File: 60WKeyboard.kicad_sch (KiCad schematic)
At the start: 59 parts, among them IC2 USBLC6-2SC6, J1 USB4215-03-A_REVA, J2 Conn_02x01_MountingPin, U1 PES12-42S-N0024, U3 nRF52840, Y1 ABM11W-32.0000MHZ-7-D1X-T3, Y2 ECS-.327-7-12-TR

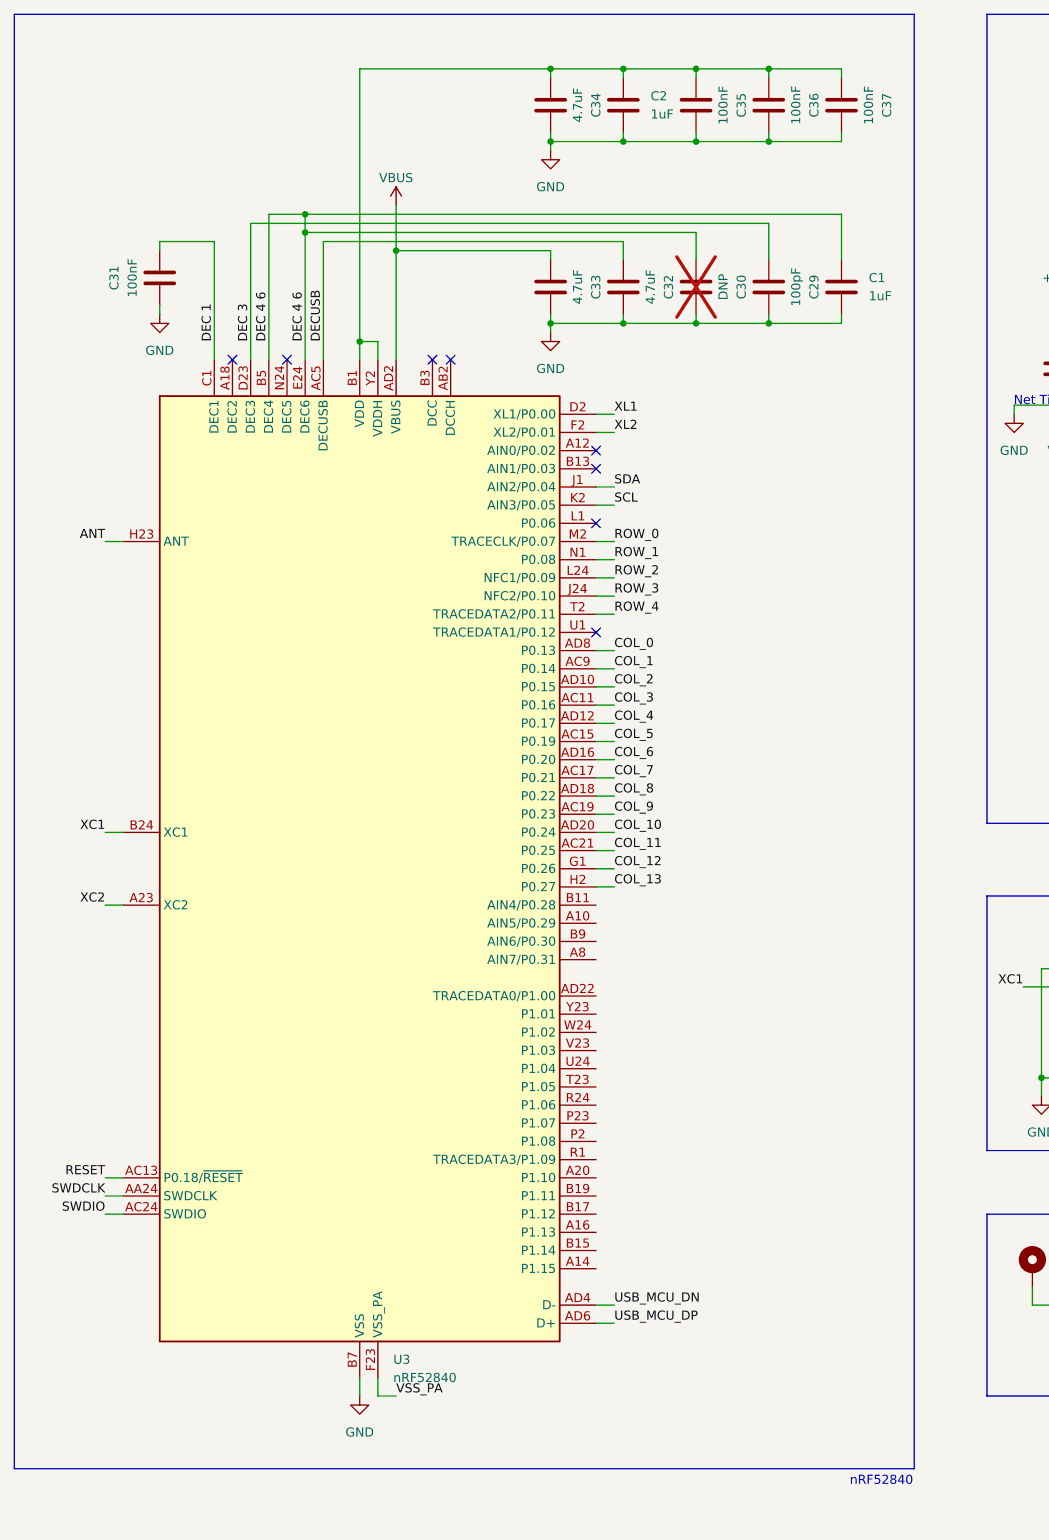
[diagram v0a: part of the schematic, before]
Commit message: v0.3
mcu power traces done
moving onto pmic
then connect key matrix
then done?
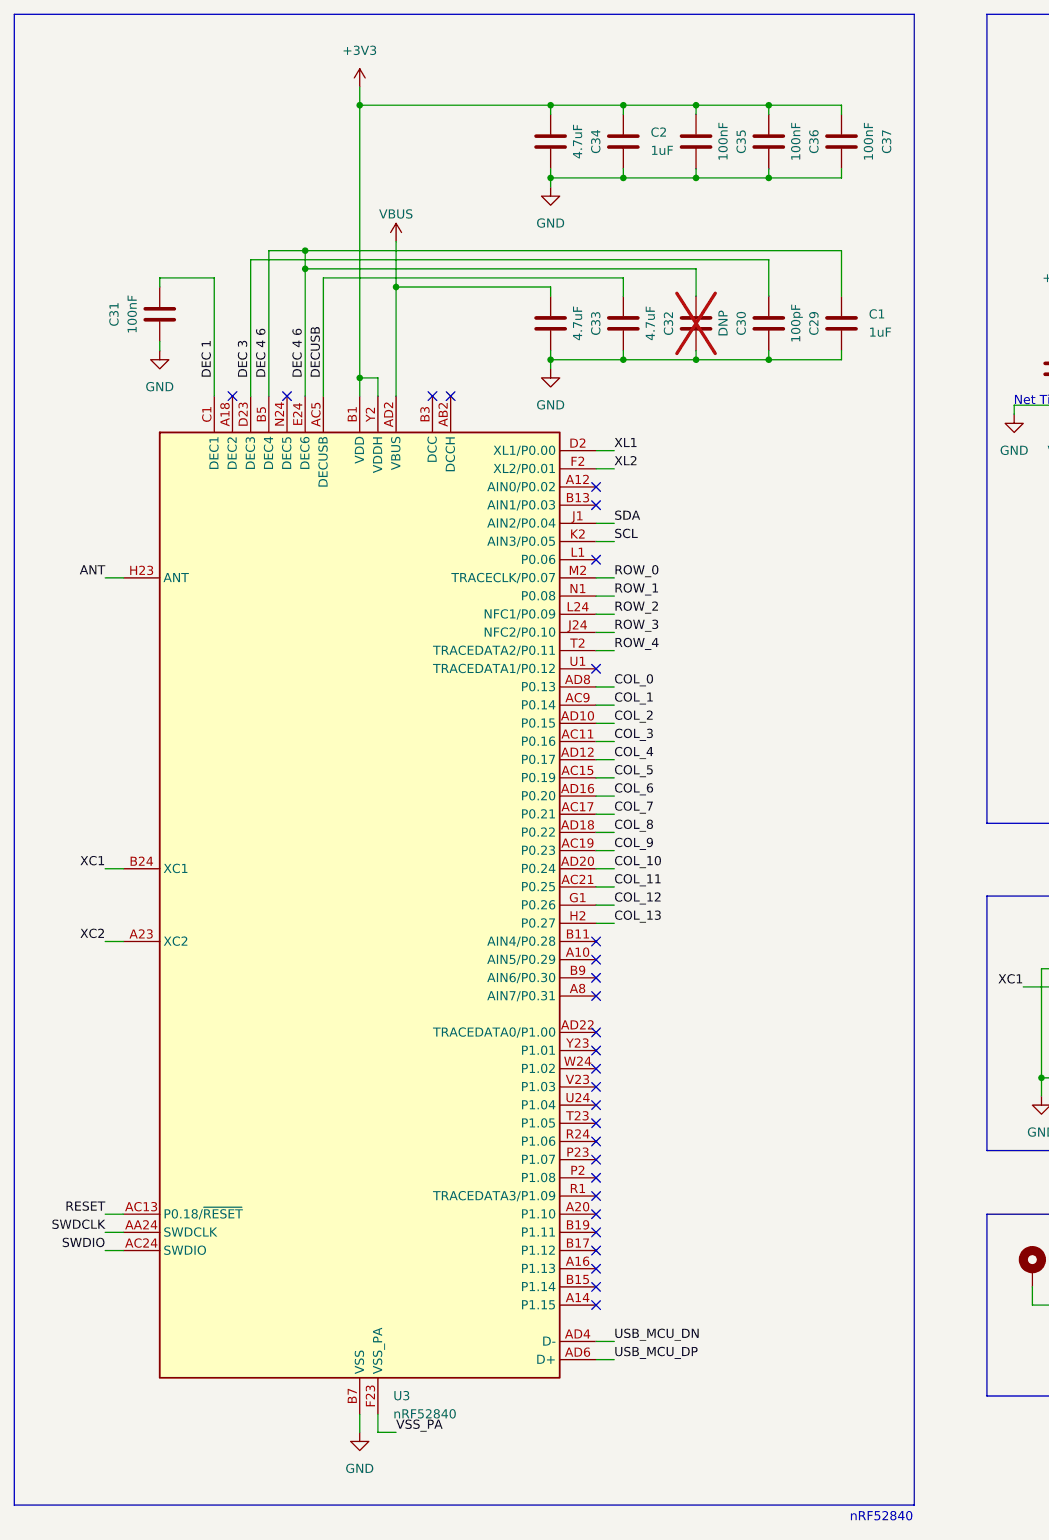
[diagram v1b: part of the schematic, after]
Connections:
- net +3V3: now also C2.2, C34.1, C35.1, C36.1, C37.1, U3.A22 (VDD), U3.AD14 (VDD), U3.AD23 (VDD), U3.B1 (VDD), U3.W1 (VDD), U3.Y2 (VDDH)
- no-connect marks 14 -> 34
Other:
- moved on the sheet: C1, C2, C29, C30, C31, C32, C33, C34, C35, C36, C37, U3

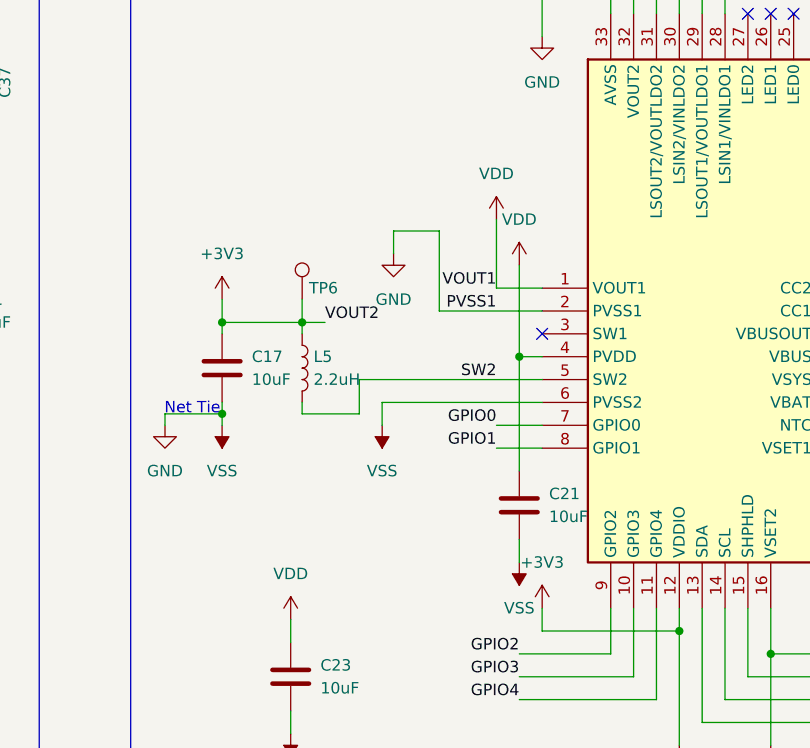
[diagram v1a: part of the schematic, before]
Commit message: v0.3
finished npm1300 routing
just columns and rows to go
get review
order
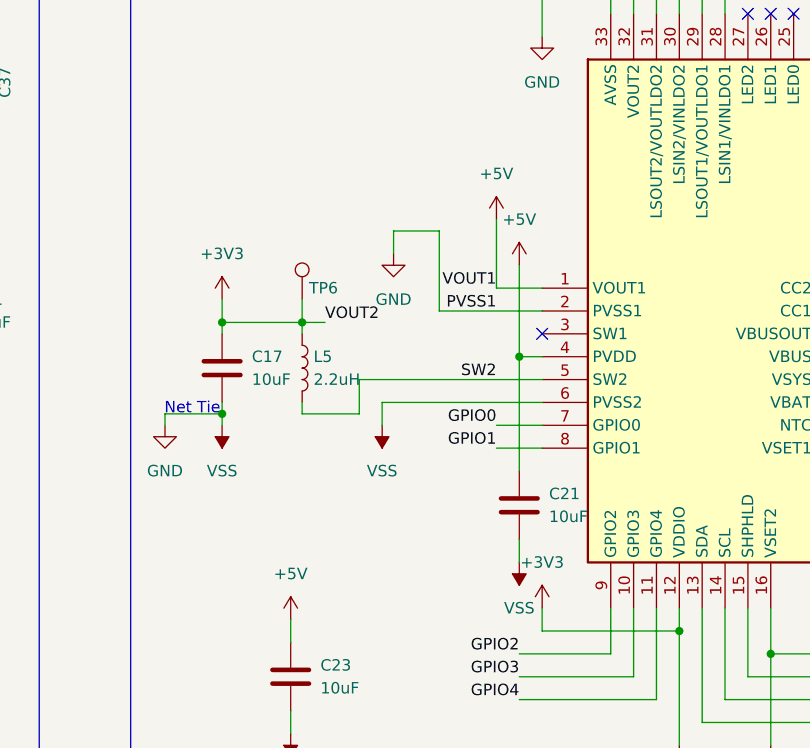
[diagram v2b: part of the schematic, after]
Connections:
- net +5V: now also C21.1, C23.1, PMIC1.1 (VOUT1), PMIC1.4 (PVDD)
- net VDD: no longer C21.1, C23.1, PMIC1.1 (VOUT1), PMIC1.4 (PVDD)

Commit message: v0.3
done
waiting for review
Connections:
- net COL_0: now also U3.AC21 (P0.25); no longer U3.AD8 (P0.13)
- net COL_1: now also U3.AC19 (P0.23); no longer U3.AC9 (P0.14)
- net COL_10: now also U3.AD16 (P0.20); no longer U3.AD20 (P0.24)
- net COL_11: now also U3.AD18 (P0.22); no longer U3.AC21 (P0.25)
- net COL_12: now also U3.AD20 (P0.24); no longer U3.G1 (P0.26)
- net COL_13: now also U3.AD22 (TRACEDATA0/P1.00); no longer U3.H2 (P0.27)
- net COL_2: now also U3.AC17 (P0.21); no longer U3.AD10 (P0.15)
- net COL_3: now also U3.AC15 (P0.19); no longer U3.AC11 (P0.16)
- net COL_4: now also U3.AC11 (P0.16); no longer U3.AD12 (P0.17)
- net COL_5: now also U3.AC9 (P0.14); no longer U3.AC15 (P0.19)
- net COL_6: now also U3.G1 (P0.26); no longer U3.AD16 (P0.20)
- net COL_7: now also U3.AD8 (P0.13); no longer U3.AC17 (P0.21)
- net COL_8: now also U3.AD10 (P0.15); no longer U3.AD18 (P0.22)
- net COL_9: now also U3.AD12 (P0.17); no longer U3.AC19 (P0.23)
- net RGB_DIN_3V3: now also U3.A16 (P1.13)
- net ROW_2: now also U3.U1 (TRACEDATA1/P0.12); no longer U3.L24 (NFC1/P0.09)
- net ROW_3: now also U3.R1 (TRACEDATA3/P1.09); no longer U3.J24 (NFC2/P0.10)
- no-connect marks 34 -> 32
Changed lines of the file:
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@@
 	)
 	(no_connect
-		(at 158.75 243.84)
-	)
-	(no_connect
 		(at 158.75 279.4)
 	)
@@
 	)
 	(no_connect
-		(at 158.75 193.04)
-	)
-	(no_connect
 		(at 138.43 154.94)
 	)
@@
 	)
 	(no_connect
+		(at 158.75 187.96)
+	)
+	(no_connect
 		(at 402.59 118.11)
 	)
@@
 	)
 	(no_connect
-		(at 158.75 266.7)
+		(at 158.75 185.42)
 	)
 	(no_connect
@@
 	)
 	(no_connect
-		(at 158.75 276.86)
-	)
-	(no_connect
 		(at 158.75 264.16)
 	)
@@
 	(wire
 		(pts
+			(xy 161.29 266.7) (xy 158.75 266.7)
+		)
+		(stroke
+			(width 0)
+			(type default)
+		)
+	)
+	(wire
+		(pts
 			(xy 276.86 111.76) (xy 276.86 109.22)
 		)
@@
 	(wire
 		(pts
-			(xy 410.21 113.03) (xy 405.13 113.03)
+			(xy 161.29 193.04) (xy 158.75 193.04)
 		)
 		(stroke
@@
 	(wire
 		(pts
-			(xy 161.29 185.42) (xy 158.75 185.42)
+			(xy 410.21 113.03) (xy 405.13 113.03)
 		)
 		(stroke
@@
 	(wire
 		(pts
+			(xy 161.29 276.86) (xy 158.75 276.86)
+		)
+		(stroke
+			(width 0)
+			(type default)
+		)
+	)
+	(wire
+		(pts
 			(xy 161.29 162.56) (xy 158.75 162.56)
 		)
@@
 	(wire
 		(pts
-			(xy 161.29 187.96) (xy 158.75 187.96)
+			(xy 466.09 250.19) (xy 466.09 261.62)
 		)
 		(stroke
@@
 	(wire
 		(pts
-			(xy 466.09 250.19) (xy 466.09 261.62)
+			(xy 425.45 234.95) (xy 425.45 237.49)
 		)
 		(stroke
@@
 	(wire
 		(pts
-			(xy 425.45 234.95) (xy 425.45 237.49)
+			(xy 161.29 243.84) (xy 158.75 243.84)
 		)
 		(stroke
@@
 	(wire
 		(pts
-			(xy 161.29 228.6) (xy 158.75 228.6)
-		)
-		(stroke
-			(width 0)
-			(type default)
-		)
-	)
-	(wire
-		(pts
 			(xy 161.29 198.12) (xy 158.75 198.12)
 		)
@@
 		)
 	)
-	(label "VOUT2"
-		(at 234.95 146.05 0)
+	(label "COL_9"
+		(at 161.29 205.74 0)
 		(effects
 			(font
@@
 		)
 	)
-	(label "COL_1"
-		(at 161.29 198.12 0)
+	(label "COL_3"
+		(at 161.29 208.28 0)
 		(effects
 			(font
@@
 		)
 	)
-	(label "COL_7"
-		(at 161.29 213.36 0)
+	(label "VOUT2"
+		(at 234.95 146.05 0)
 		(effects
 			(font
@@
 		)
 	)
-	(label "GPIO0"
-		(at 254 157.48 180)
+	(label "COL_1"
+		(at 161.29 218.44 0)
 		(effects
 			(font
 				(size 1.27 1.27)
 			)
-			(justify right bottom)
+			(justify left bottom)
 		)
 	)
-	(label "GPIO2"
-		(at 256.54 182.88 180)
+	(label "GPIO0"
+		(at 254 157.48 180)
 		(effects
 			(font
@@
 		)
 	)
-	(label "COL_4"
-		(at 161.29 205.74 0)
+	(label "GPIO2"
+		(at 256.54 182.88 180)
 		(effects
 			(font
 				(size 1.27 1.27)
 			)
-			(justify left bottom)
+			(justify right bottom)
 		)
 	)
@@
 		)
 	)
+	(label "COL_8"
+		(at 161.29 200.66 0)
+		(effects
+			(font
+				(size 1.27 1.27)
+			)
+			(justify left bottom)
+		)
+	)
 	(label "ROW_2"
 		(at 508 113.03 0)
@@
 		)
 	)
-	(label "ROW_3"
-		(at 161.29 187.96 0)
+	(label "COL_10"
+		(at 161.29 210.82 0)
 		(effects
 			(font
@@
 		)
 	)
-	(label "PVSS1"
-		(at 254 144.78 180)
-		(effects
-			(font
-				(size 1.27 1.27)
-			)
-			(justify right bottom)
-		)
-	)
-	(label "USB_DN"
-		(at 405.13 120.65 0)
+	(label "COL_13"
+		(at 161.29 243.84 0)
 		(effects
 			(font
@@
 		)
 	)
-	(label "COL_9"
-		(at 161.29 218.44 0)
+	(label "COL_12"
+		(at 161.29 220.98 0)
 		(effects
 			(font
@@
 		)
 	)
-	(label "COL_0"
-		(at 161.29 195.58 0)
+	(label "PVSS1"
+		(at 254 144.78 180)
 		(effects
 			(font
 				(size 1.27 1.27)
 			)
-			(justify left bottom)
+			(justify right bottom)
 		)
 	)
-	(label "COL_8"
-		(at 161.29 215.9 0)
+	(label "USB_DN"
+		(at 405.13 120.65 0)
 		(effects
 			(font
@@
 		)
 	)
-	(label "COL_10"
-		(at 161.29 220.98 0)
-		(effects
-			(font
-				(size 1.27 1.27)
-			)
-			(justify left bottom)
-		)
-	)
 	(label "VOUT2"
 		(at 259.08 106.68 180)
@@
 		)
 	)
-	(label "CC2"
-		(at 405.13 125.73 0)
+	(label "COL_5"
+		(at 161.29 198.12 0)
 		(effects
 			(font
@@
 		)
 	)
-	(label "COL_3"
-		(at 161.29 203.2 0)
+	(label "CC2"
+		(at 405.13 125.73 0)
 		(effects
 			(font
@@
 		)
 	)
+	(label "ROW_3"
+		(at 161.29 266.7 0)
+		(effects
+			(font
+				(size 1.27 1.27)
+			)
+			(justify left bottom)
+		)
+	)
 	(label "USB_MCU_DP"
 		(at 161.29 289.56 0)
@@
 		)
 	)
+	(label "COL_7"
+		(at 161.29 195.58 0)
+		(effects
+			(font
+				(size 1.27 1.27)
+			)
+			(justify left bottom)
+		)
+	)
 	(label "XL2"
 		(at 303.53 234.95 0)
@@
 		)
 	)
-	(label "COL_2"
-		(at 161.29 200.66 0)
+	(label "COL_6"
+		(at 161.29 226.06 0)
 		(effects
 			(font
@@
 		)
 	)
-	(label "COL_13"
-		(at 161.29 228.6 0)
+	(label "COL_2"
+		(at 161.29 213.36 0)
 		(effects
 			(font
@@
 		)
 	)
+	(label "ROW_2"
+		(at 161.29 193.04 0)
+		(effects
+			(font
+				(size 1.27 1.27)
+			)
+			(justify left bottom)
+		)
+	)
 	(label "COL_9"
 		(at 482.6 130.81 180)
@@
 		)
 	)
-	(label "COL_6"
-		(at 161.29 210.82 0)
-		(effects
-			(font
-				(size 1.27 1.27)
-			)
-			(justify left bottom)
-		)
-	)
 	(label "RGB_DIN_3V3"
 		(at 496.57 161.29 0)
@@
 		)
 	)
-	(label "ROW_2"
-		(at 161.29 185.42 0)
-		(effects
-			(font
-				(size 1.27 1.27)
-			)
-			(justify left bottom)
-		)
-	)
-	(label "COL_12"
-		(at 161.29 226.06 0)
+	(label "RGB_DIN_3V3"
+		(at 161.29 276.86 0)
 		(effects
 			(font
@@
 		)
 	)
-	(label "COL_11"
-		(at 161.29 223.52 0)
-		(effects
-			(font
-				(size 1.27 1.27)
-			)
-			(justify left bottom)
-		)
-	)
 	(label "DEC 3"
 		(at 110.49 152.4 90)
@@
 		)
 	)
-	(label "COL_5"
-		(at 161.29 208.28 0)
+	(label "VBUS"
+		(at 297.18 149.86 0)
 		(effects
 			(font
@@
 		)
 	)
-	(label "VBUS"
-		(at 297.18 149.86 0)
+	(label "XC2"
+		(at 266.7 234.95 0)
 		(effects
 			(font
@@
 		)
 	)
-	(label "XC2"
-		(at 266.7 234.95 0)
+	(label "COL_4"
+		(at 161.29 203.2 0)
 		(effects
 			(font
@@
 		)
 	)
+	(label "COL_11"
+		(at 161.29 215.9 0)
+		(effects
+			(font
+				(size 1.27 1.27)
+			)
+			(justify left bottom)
+		)
+	)
 	(label "RESET"
 		(at 90.17 269.24 180)
@@
 		)
 	)
+	(label "COL_0"
+		(at 161.29 223.52 0)
+		(effects
+			(font
+				(size 1.27 1.27)
+			)
+			(justify left bottom)
+		)
+	)

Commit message: v0.3
finally finished
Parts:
- added C16: 1.5pF, Capacitor_SMD:C_0201_0603Metric, symbol Device:C
- added J3: Conn_01x04_Socket, Connector_PinSocket_2.54mm:PinSocket_1x04_P2.54mm_Vertical, symbol Connector:Conn_01x04_Socket
- added L6: 3.9nH, Inductor_SMD:L_0201_0603Metric, symbol Device:L
- TP5: now not fitted
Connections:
- net GND: now also C16.2, J3.4 (Pin_4)
- net RESET: now also J3.3 (Pin_3)
- net RF: now also L6.2; no longer L4.2
- net SWDCLK: now also J3.2 (Pin_2)
- net SWDIO: now also J3.1 (Pin_1)
- net VBUS: no longer C33.1, U3.AD2 (VBUS)
- net VDD: now also C33.1, U3.AD2 (VBUS)
- new net: C16.1, L4.2, L6.1
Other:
- note added: "SWD"
- moved on the sheet: C10, C11, C25, C26, E1, L3, L4, R4, R5, R6, R7, U1
